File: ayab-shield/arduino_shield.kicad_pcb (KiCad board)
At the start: 2 copper layers, 73.1 x 53.3 mm, 35 parts, among them IC1 ULN2803A, IC2 ULN2803A, IC3 MCP2300X/P, IC4 MCP2300X/P, J1 Power, J2 Digital/PWM, J3 Analog, J4 Digital/PWM, X1 KLDX-0202-AC

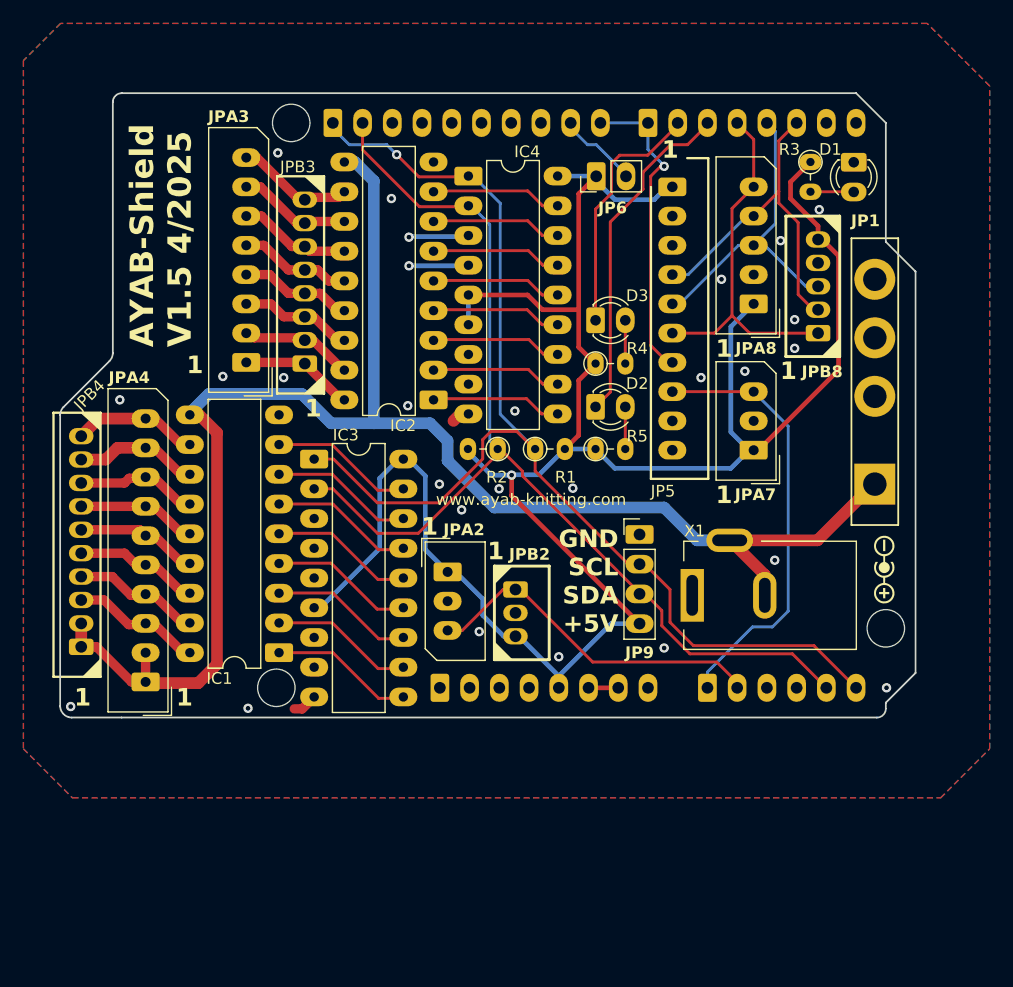
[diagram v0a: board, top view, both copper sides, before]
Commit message: Fix orientation of solenoid headers on schematic and PCB
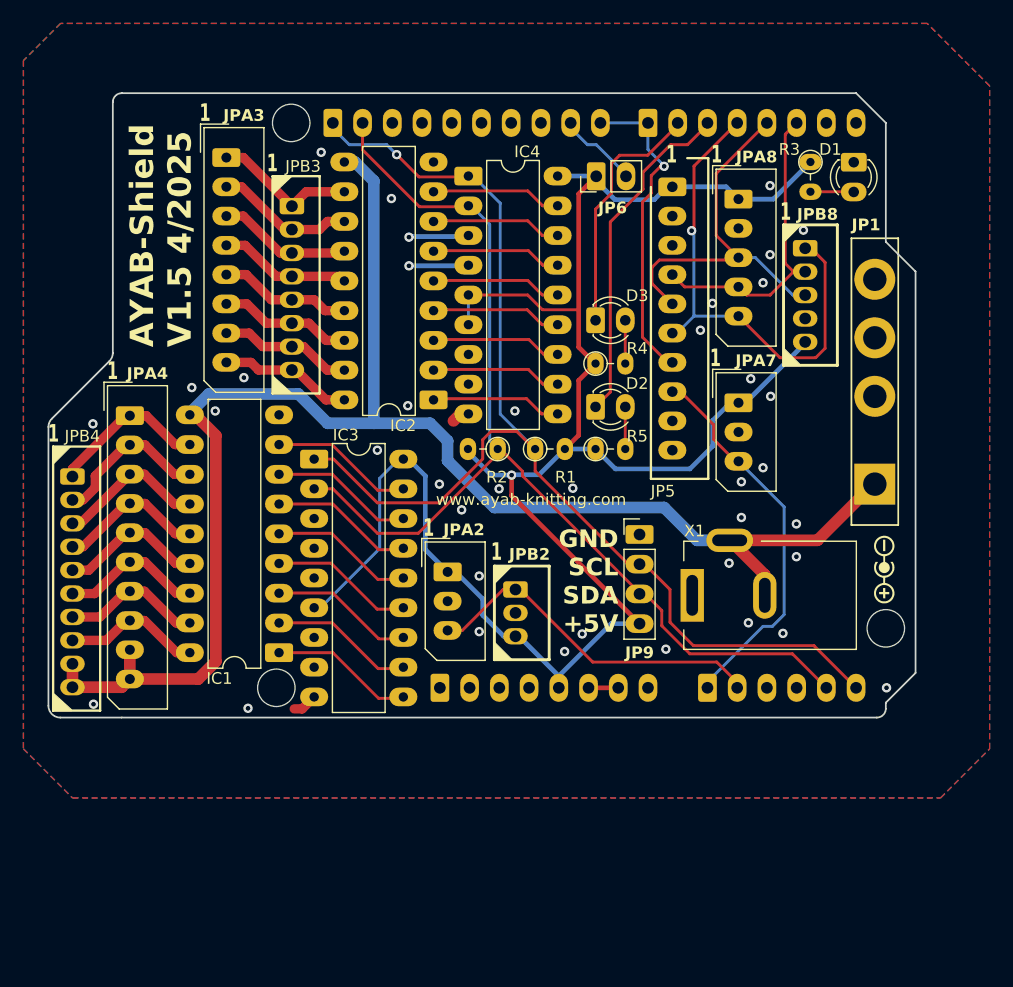
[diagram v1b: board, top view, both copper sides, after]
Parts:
- moved JPA4 22.8 mm to (116.2, 104.2), turned to -90 degrees
- moved JPA3 17.6 mm to (124.4, 82.2), turned to -90 degrees
- moved JPB4 14.6 mm to (111.2, 109.5), turned to 90 degrees
- moved JPB3 13.5 mm to (130.0, 86.3), turned to 90 degrees
- moved JPA8 9.04 mm to (168.2, 85.8), turned to -90 degrees
- moved JPA7 4.25 mm to (168.2, 103.2), turned to -90 degrees
- moved JPB8 1.33 mm to (173.8, 94.0), turned to 90 degrees
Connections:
- JPA3 pad 1: Net-(IC2-O1) -> Net-(IC2-O8)
- JPA3 pad 2: Net-(IC2-O2) -> Net-(IC2-O7)
- JPA3 pad 3: Net-(IC2-O3) -> Net-(IC2-O6)
- JPA3 pad 4: Net-(IC2-O4) -> Net-(IC2-O5)
- JPA3 pad 5: Net-(IC2-O5) -> Net-(IC2-O4)
- JPA3 pad 6: Net-(IC2-O6) -> Net-(IC2-O3)
- JPA3 pad 7: Net-(IC2-O7) -> Net-(IC2-O2)
- JPA3 pad 8: Net-(IC2-O8) -> Net-(IC2-O1)
- JPA4 pad 1: +15V -> Net-(IC1-O8)
- JPA4 pad 10: Net-(IC1-O8) -> +15V
- JPA4 pad 2: +15V -> Net-(IC1-O7)
- JPA4 pad 3: Net-(IC1-O1) -> Net-(IC1-O6)
- JPA4 pad 4: Net-(IC1-O2) -> Net-(IC1-O5)
- JPA4 pad 5: Net-(IC1-O3) -> Net-(IC1-O4)
- JPA4 pad 6: Net-(IC1-O4) -> Net-(IC1-O3)
- JPA4 pad 7: Net-(IC1-O5) -> Net-(IC1-O2)
- JPA4 pad 8: Net-(IC1-O6) -> Net-(IC1-O1)
- JPA4 pad 9: Net-(IC1-O7) -> +15V
- JPB3 pad 1: Net-(IC2-O1) -> Net-(IC2-O8)
- JPB3 pad 2: Net-(IC2-O2) -> Net-(IC2-O7)
- JPB3 pad 3: Net-(IC2-O3) -> Net-(IC2-O6)
- JPB3 pad 4: Net-(IC2-O4) -> Net-(IC2-O5)
- JPB3 pad 5: Net-(IC2-O5) -> Net-(IC2-O4)
- JPB3 pad 6: Net-(IC2-O6) -> Net-(IC2-O3)
- JPB3 pad 7: Net-(IC2-O7) -> Net-(IC2-O2)
- JPB3 pad 8: Net-(IC2-O8) -> Net-(IC2-O1)
- JPB4 pad 1: +15V -> Net-(IC1-O8)
- JPB4 pad 10: Net-(IC1-O8) -> +15V
- JPB4 pad 2: +15V -> Net-(IC1-O7)
- JPB4 pad 3: Net-(IC1-O1) -> Net-(IC1-O6)
- JPB4 pad 4: Net-(IC1-O2) -> Net-(IC1-O5)
- JPB4 pad 5: Net-(IC1-O3) -> Net-(IC1-O4)
- JPB4 pad 6: Net-(IC1-O4) -> Net-(IC1-O3)
- JPB4 pad 7: Net-(IC1-O5) -> Net-(IC1-O2)
- JPB4 pad 8: Net-(IC1-O6) -> Net-(IC1-O1)
- JPB4 pad 9: Net-(IC1-O7) -> +15V
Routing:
- net +5V: track 193.4 -> 171.6 mm
- net /ENC_C: track 31.8 -> 43.5 mm, vias 0 -> 1
- net /ENC_B: track 27.8 -> 33.0 mm
- net /EOL_R: track 37.3 -> 33.0 mm
- net /ENC_A: track 30.3 -> 26.3 mm
- net Net-(IC1-O7): track 10.6 -> 13.6 mm
- net Net-(IC1-O6): track 10.1 -> 12.8 mm
- net Net-(IC1-O8): track 10.8 -> 13.6 mm
- net Net-(IC1-O5): track 9.95 -> 12.6 mm
- net Net-(IC1-O4): track 10.2 -> 12.4 mm
- net Net-(IC2-O7): track 9.72 -> 11.9 mm
- net Net-(IC2-O8): track 10.2 -> 12.3 mm
- net Net-(IC1-O3): track 10.4 -> 12.3 mm
- net Net-(IC2-O6): track 9.62 -> 11.4 mm
- net Net-(IC2-O3): track 9.67 -> 11.4 mm
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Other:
- board size 73.1 x 53.3 mm -> 74.1 x 53.3 mm

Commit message: Replace footprints (DRC errors not corrected)
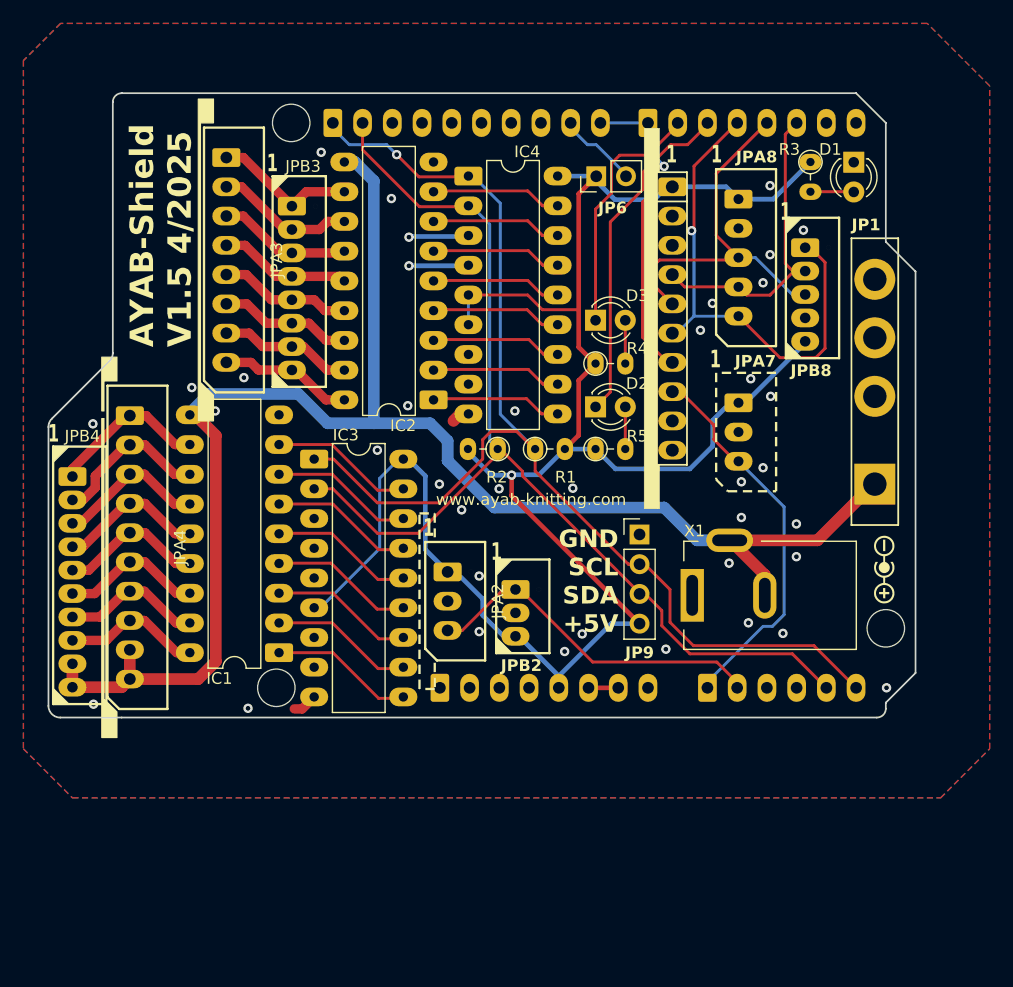
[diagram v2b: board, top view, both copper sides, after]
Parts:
- JP5: footprint ayab-library:SHDR10W70P0X250_1X10_2740X490X590P -> ayab-library:HNC2-2.5P-10DS
- JPA2: footprint ayab-library:Molex_SPOX_5267-03A_1x03_P2.50mm_Vertical -> ayab-library:Molex_0022035035_or_Hirose_HNC2-2.5P-3DS_(dashed_bar)
- JPA3: footprint ayab-library:Molex_SPOX_5267-08A_1x08_P2.50mm_Vertical -> ayab-library:Molex_0022035085_or_Hirose_HNC2_2.5P_8DS
- JPA4: footprint ayab-library:Molex_SPOX_5267-10A_1x10_P2.50mm_Vertical -> ayab-library:Molex_0022035105_or_Hirose_HNC2-2.5P-10DS
- JPA7: footprint ayab-library:Molex_SPOX_5267-03A_1x03_P2.50mm_Vertical -> ayab-library:Molex_SPOX_5267-03A_1x03_P2.50mm_Vertical_(dashed_outline)
- JPB2: footprint ayab-library:CONN-TH_3P-P2.00_A2004WV-3P -> ayab-library:530140310
- JPB8: footprint ayab-library:CONN-TH_A2004WV-5P -> ayab-library:530140510
- moved JP5 22.5 mm to (162.5, 84.7), turned to -90 degrees
- moved JPB8 4.05 mm to (173.8, 89.9)
- moved JPB2 2.00 mm to (149.1, 119.1)

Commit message: Squeeze everything onto a normal size shield
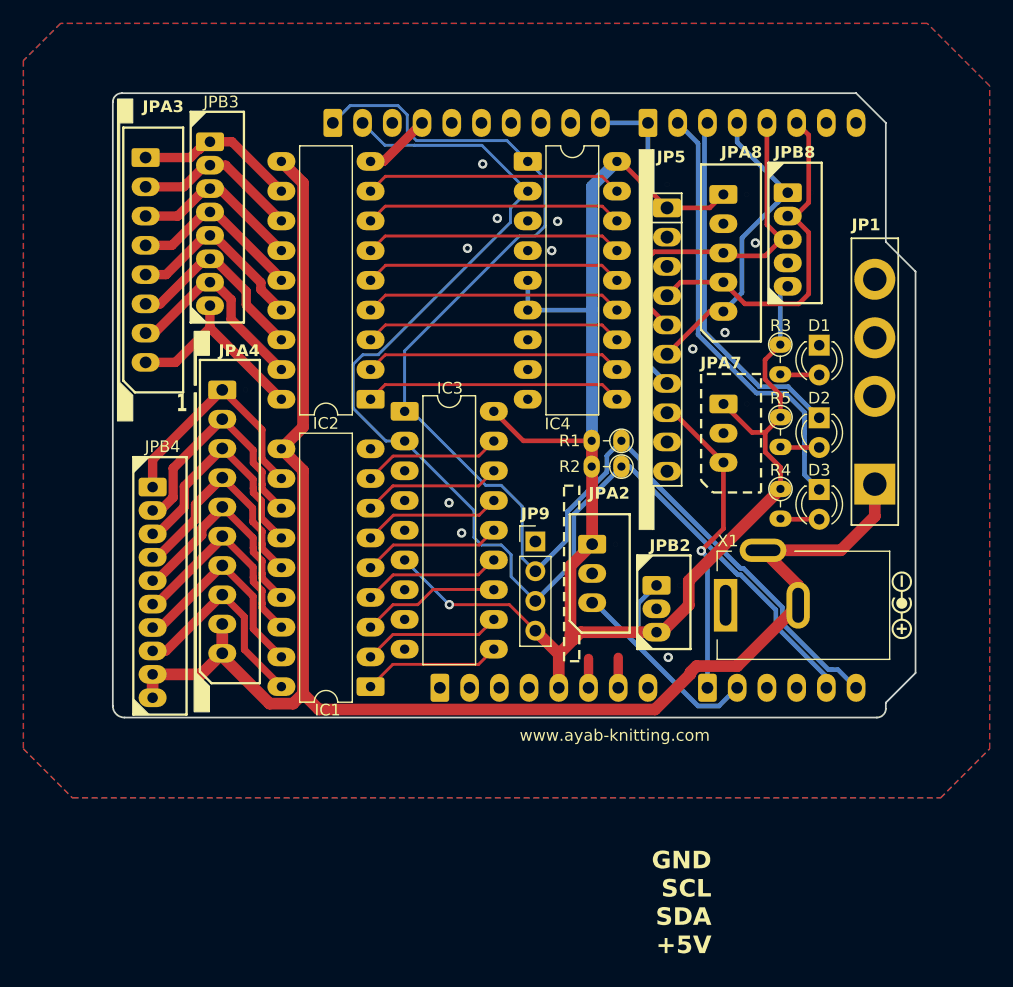
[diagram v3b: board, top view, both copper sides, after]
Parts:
- removed JP6: 1x2 2.5mm, ayab-library:PinHeader_1x02_P2.54mm_Vertical
- removed MH1, MH2, MH4: MountingHole_3.2mm, ayab-library:MountingHole_3.2mm
- removed REF**: OSHW-Symbol_6.7x6mm_SilkScreen, Symbol:OSHW-Symbol_6.7x6mm_SilkScreen
- moved D3 24.0 mm to (175.1, 110.6), turned to -90 degrees
- moved D2 19.1 mm to (175.1, 104.4), turned to -90 degrees
- moved R4 19.1 mm to (171.7, 110.5), turned to -90 degrees
- moved R5 16.0 mm to (171.7, 104.4), turned to -90 degrees
- moved D1 15.9 mm to (175.1, 98.2)
- moved R3 15.8 mm to (171.7, 98.2)
- moved JPA2 12.6 mm to (155.7, 115.2)
- moved JPB2 12.1 mm to (161.2, 118.8)
- moved R2 10.7 mm to (158.2, 108.6)
- moved JP9 8.92 mm to (150.8, 115.0)
- moved JPB3 8.90 mm to (123.0, 80.8)
- moved IC3 8.74 mm to (139.6, 103.9)
- moved IC1 8.34 mm to (136.7, 127.4)
- moved JPA4 8.20 mm to (124.0, 102.0)
- moved R1 7.40 mm to (158.2, 106.4), turned to 180 degrees
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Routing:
- net +5V: track 171.6 -> 141.0 mm
- net /ENC_C: track 43.5 -> 26.5 mm, vias 1 -> 0
- net /LED_GRN: track 21.2 -> 37.8 mm
- net /SDA: track 93.4 -> 108.1 mm
- net Net-(IC2-I5): track 11.1 -> 22.1 mm
- net Net-(IC2-I2): track 11.1 -> 22.1 mm
- net Net-(IC2-I6): track 11.1 -> 22.1 mm
- net Net-(IC2-I4): track 11.2 -> 22.1 mm
- net Net-(IC2-I7): track 11.1 -> 22.1 mm
- net Net-(IC2-I3): track 11.2 -> 22.1 mm
- net Net-(IC2-I8): track 11.2 -> 22.1 mm
- net Net-(IC2-I1): track 11.2 -> 22.1 mm
- net /SCL: track 102.9 -> 111.6 mm, vias 1 -> 0
- net /EOL_L: track 30.4 -> 22.6 mm
- net /BUZZ: track 6.96 -> 0.00 mm
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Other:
- board size 74.1 x 53.3 mm -> 68.6 x 53.3 mm
- board text removed: "AYAB-Shield V1.5 4/2025"
- board text removed: "CC-BY-SA 4.0"

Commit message: Horizontal axial resistors R1 and R2
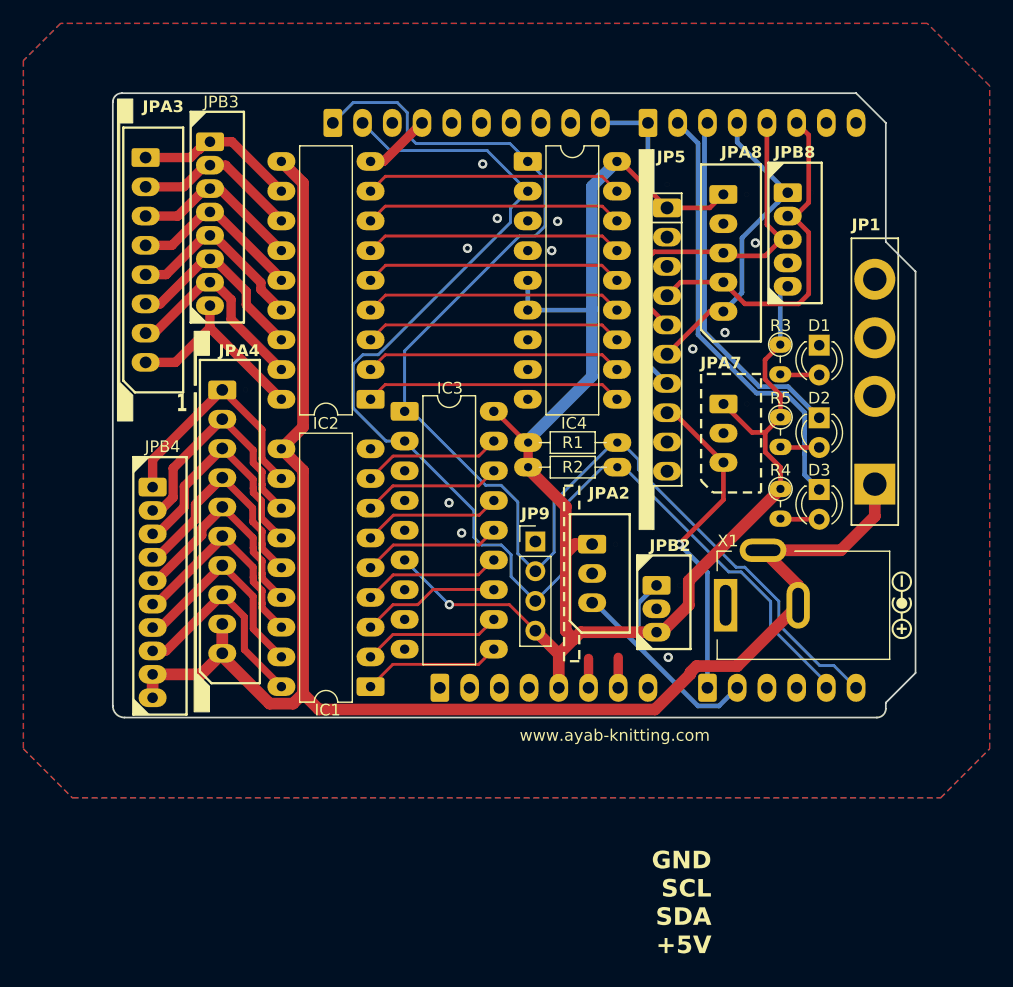
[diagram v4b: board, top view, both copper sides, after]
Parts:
- R1, R2: footprint ayab-library:R_Axial_DIN0204_L3.6mm_D1.6mm_P2.54mm_Vertical -> ayab-library:R_Axial_DIN0204_L3.6mm_D1.6mm_P7.62mm_Horizontal
- moved R1 0.38 mm to (157.8, 106.5)
- moved R2 0.35 mm to (157.8, 108.7)
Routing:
- net /EOL_R: track 26.8 -> 28.4 mm
- net /SDA: track 108.1 -> 109.1 mm
- net /SCL: track 111.6 -> 112.5 mm

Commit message: Switch I2C header to Stemma connector (JST PH) and pinout
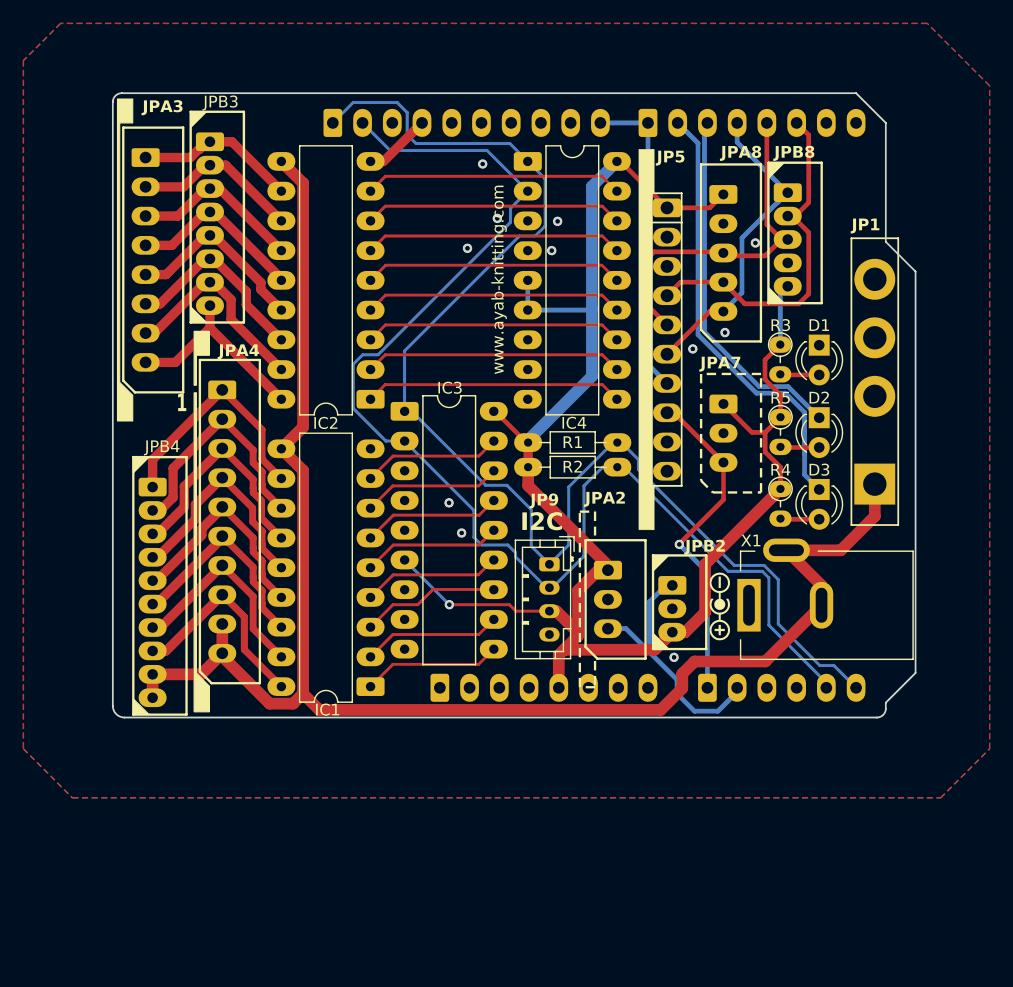
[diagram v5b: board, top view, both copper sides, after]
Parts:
- JP9: footprint ayab-library:PinHeader_1x04_P2.54mm_Vertical -> Connector_JST:JST_PH_B4B-PH-K_1x04_P2.00mm_Vertical
- moved G*** 15.6 mm to (166.6, 120.5)
- moved JPA2 2.60 mm to (157.0, 117.5)
- moved JP9 2.29 mm to (152.0, 117.0), turned to -90 degrees
- moved X1 2.00 mm to (169.1, 120.5)
- moved JPB2 1.35 mm to (162.5, 118.8)
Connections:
- J2 pad 9: /BUZZ -> unconnected-(J2-Pin_9-Pad9)
- JP9 pad 1: GND -> /SCL
- JP9 pad 2: /SCL -> /SDA
- JP9 pad 3: /SDA -> +5V
- JP9 pad 4: +5V -> GND
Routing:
- net GND: track 10.9 -> 5.76 mm
- net +5V: track 141.1 -> 145.4 mm
- net +15V: track 134.2 -> 134.9 mm
- net /SDA: track 109.1 -> 108.6 mm
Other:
- board text added: "I2C"
- board text removed: "GND SCL SDA +5V"

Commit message: Reroute paths and move dots in connector footprints
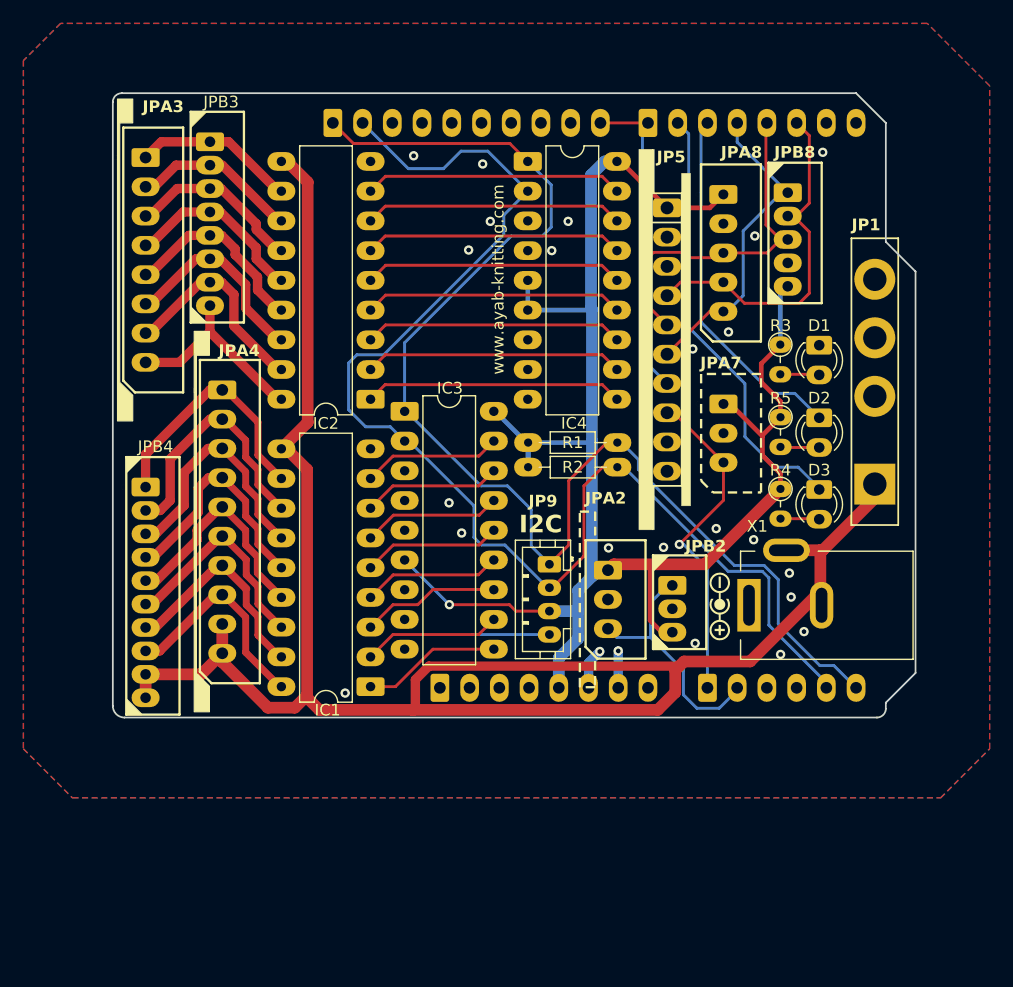
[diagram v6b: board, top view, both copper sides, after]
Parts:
- D1, D2, D3: footprint ayab-library:LED_D3.0mm -> ayab-library:LED_D3.0mm_LongPads
- JP9: footprint Connector_JST:JST_PH_B4B-PH-K_1x04_P2.00mm_Vertical -> ayab-library:JST_PH_B4B-PH-K_1x04_P2.00mm_Vertical_LongPads
- moved JPB4 0.60 mm to (117.5, 110.3)
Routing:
- net +15V: track 134.9 -> 162.1 mm
- net GND: track 5.76 -> 13.3 mm, vias 11 -> 24
- net +5V: track 145.4 -> 148.8 mm
- net /SDA: track 108.6 -> 111.2 mm
- net Net-(IC1-O7): track 20.3 -> 21.7 mm
- net Net-(IC1-O6): track 19.7 -> 21.0 mm
- net /EOL_L: track 22.6 -> 21.5 mm
- net Net-(IC1-O5): track 19.3 -> 20.3 mm
- net Net-(IC1-O8): track 20.4 -> 21.5 mm
- net /SCL: track 112.7 -> 111.7 mm
- net Net-(IC1-O4): track 18.8 -> 19.6 mm
- net Net-(IC1-O1): track 17.9 -> 18.6 mm
- net Net-(IC1-O2): track 18.0 -> 18.8 mm
- net Net-(IC2-O2): track 17.5 -> 18.1 mm
- net Net-(IC2-O4): track 16.0 -> 16.6 mm
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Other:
- board text removed: "1"
